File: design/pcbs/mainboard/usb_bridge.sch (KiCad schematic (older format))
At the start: 4 parts, among them U18 Combo384, U6 Si8645BA-B-IU

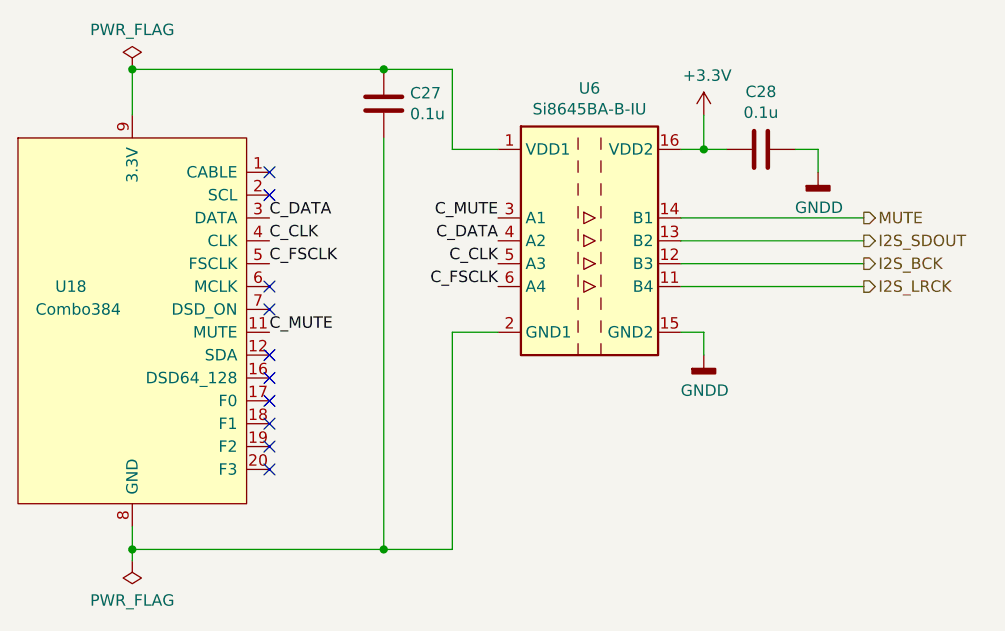
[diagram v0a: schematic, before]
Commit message: Renumbered footprints to follow board position.
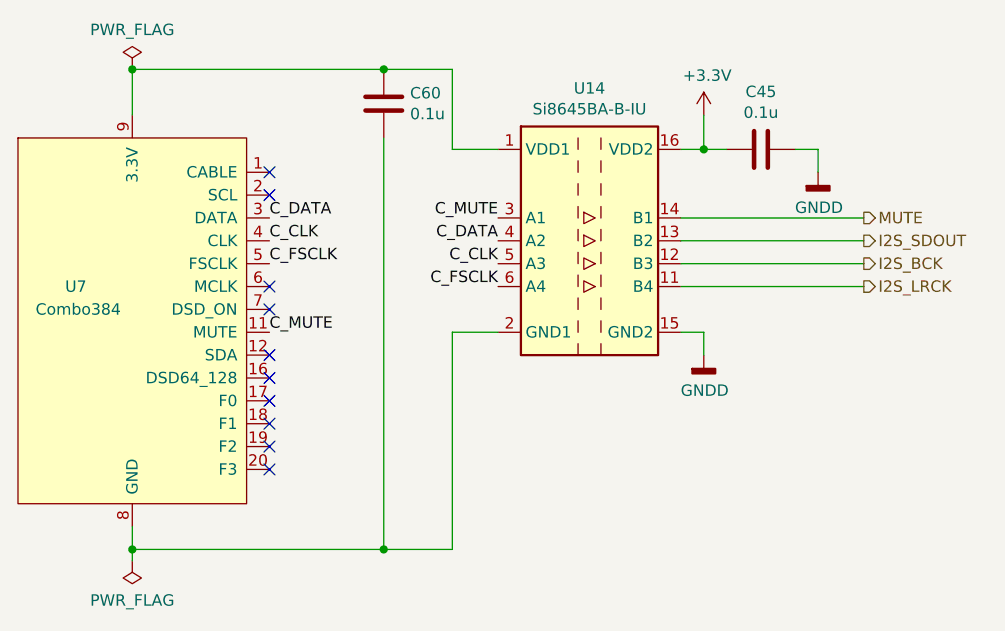
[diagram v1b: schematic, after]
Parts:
- renumbered C28 to C45, C27 to C60, U6 to U14, U18 to U7
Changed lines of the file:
@@
 P 6600 3750
 AR Path="/5ECBF549" Ref="U?"  Part="1"
-AR Path="/5EC79CC1/5ECBF549" Ref="U6"  Part="1"
-F 0 "U6" H 6600 4417 50  0000 C CNN
+AR Path="/5EC79CC1/5ECBF549" Ref="U14"  Part="1"
+F 0 "U14" H 6600 4417 50  0000 C CNN
 F 1 "Si8645BA-B-IU" H 6600 4326 50  0000 C CNN
 F 2 "Package_SO:QSOP-16_3.9x4.9mm_P0.635mm" H 6600 3200 50  0001 C CIN
@@
 	7100 4150 7100 4250
 $Comp
-L Device:C C27
+L Device:C C60
 U 1 1 5ECC76CF
 P 5700 3150
-F 0 "C27" H 5815 3196 50  0000 L CNN
+F 0 "C60" H 5815 3196 50  0000 L CNN
 F 1 "0.1u" H 5815 3105 50  0000 L CNN
 F 2 "Capacitor_SMD:C_0603_1608Metric" H 5738 3000 50  0001 C CNN
@@
 $EndComp
 $Comp
-L Device:C C28
+L Device:C C45
 U 1 1 5ECCB7E4
 P 7350 3350
-F 0 "C28" V 7098 3350 50  0000 C CNN
+F 0 "C45" V 7098 3350 50  0000 C CNN
 F 1 "0.1u" V 7189 3350 50  0000 C CNN
 F 2 "Capacitor_SMD:C_0603_1608Metric" H 7388 3200 50  0001 C CNN
@@
 	5700 5100 6000 5100
 $Comp
-L dac:Combo384 U18
+L dac:Combo384 U7
 U 1 1 5F2DBC25
 P 4600 4100
-F 0 "U18" H 4400 4250 50  0000 R CNN
+F 0 "U7" H 4400 4250 50  0000 R CNN
 F 1 "Combo384" H 4550 4150 50  0000 R CNN
 F 2 "mainboard:AmaneroCombo384" H 4800 4300 50  0001 C CNN
